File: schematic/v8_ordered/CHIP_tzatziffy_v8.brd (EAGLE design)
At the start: 40.9 x 49.8 mm, 61 parts, among them J1 2X20-CHIP0.8_DRILL_0.15OFFSET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, J2 USB-MICROB", Q2 n.a. / 2N7002ET1G, U1 n.a. / LMR62421, U3 DS2431P, X1 FH12-40S-0.5SH

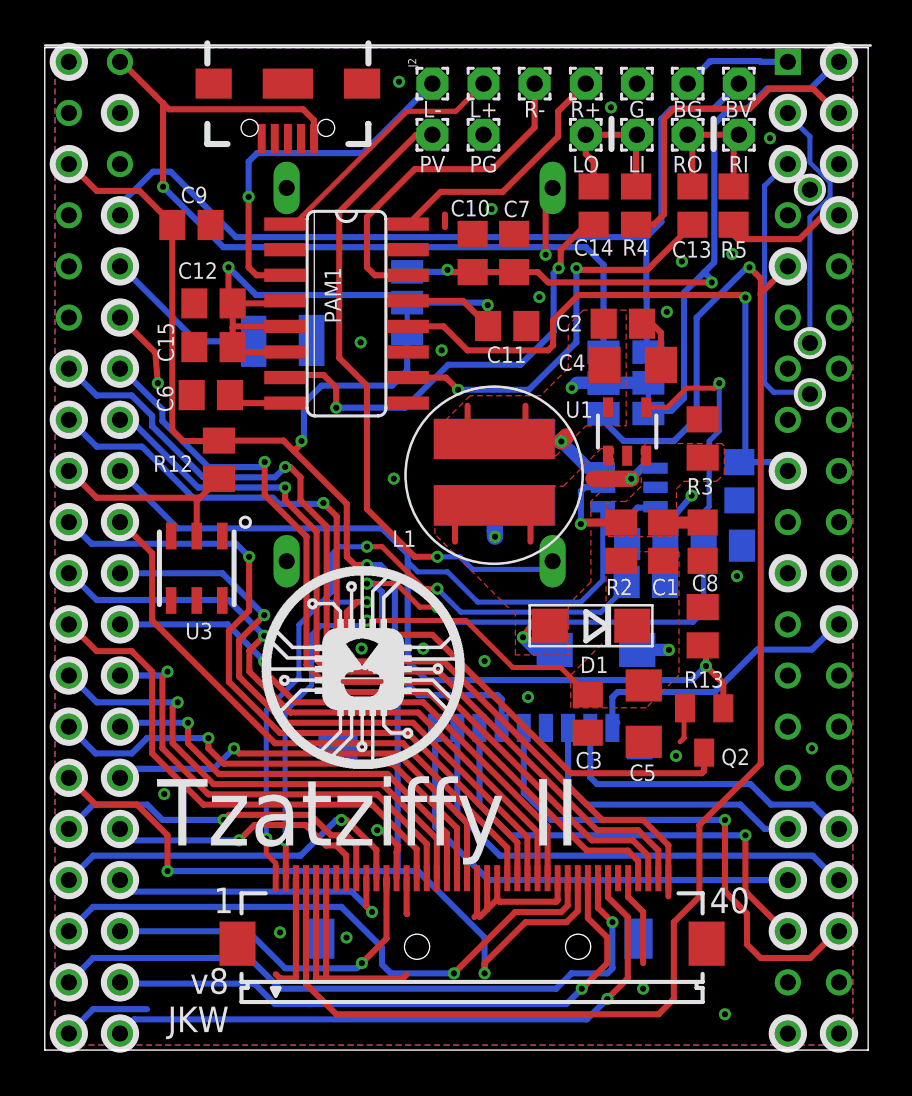
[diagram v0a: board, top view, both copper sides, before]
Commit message: changed chip footprint to clamp via row claming 0.1mm outside and ordered v8
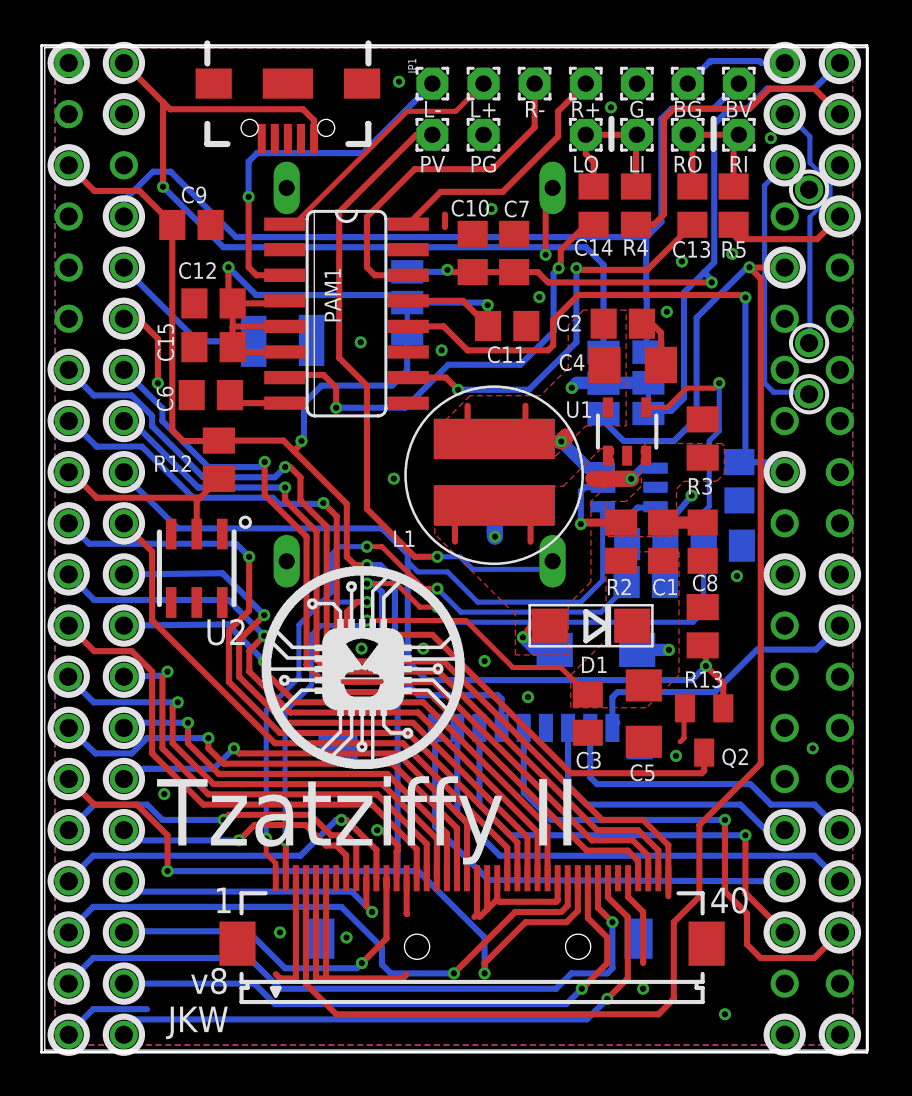
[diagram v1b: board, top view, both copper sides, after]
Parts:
- removed U3: DS2431P, Keyboard v0_5:TSOC6
- added U2: DS2431P, JKW_CHIP:TSOC6
- J1: value 2X20-CHIP0.8_DRILL_0.15OFFSET_LR -> 2X20-CHIP0.9DRILLS_2; device JKW_CHIP:2X20CHIP_0.15MM_OFFSET_TH_08 -> JKW_CHIP:2X20CHIP_BANK_OFFSET_TH_0.9
- JP1: value USB-MICROB" -> USBMICRO_SMD
- renumbered J2 to JP1
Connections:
- net 1WIRE: now also U2.2; no longer U3.2
- net GND: now also U2.1; no longer U3.1
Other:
- board size 40.9 x 49.8 mm -> 41 x 50 mm

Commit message: added and gate
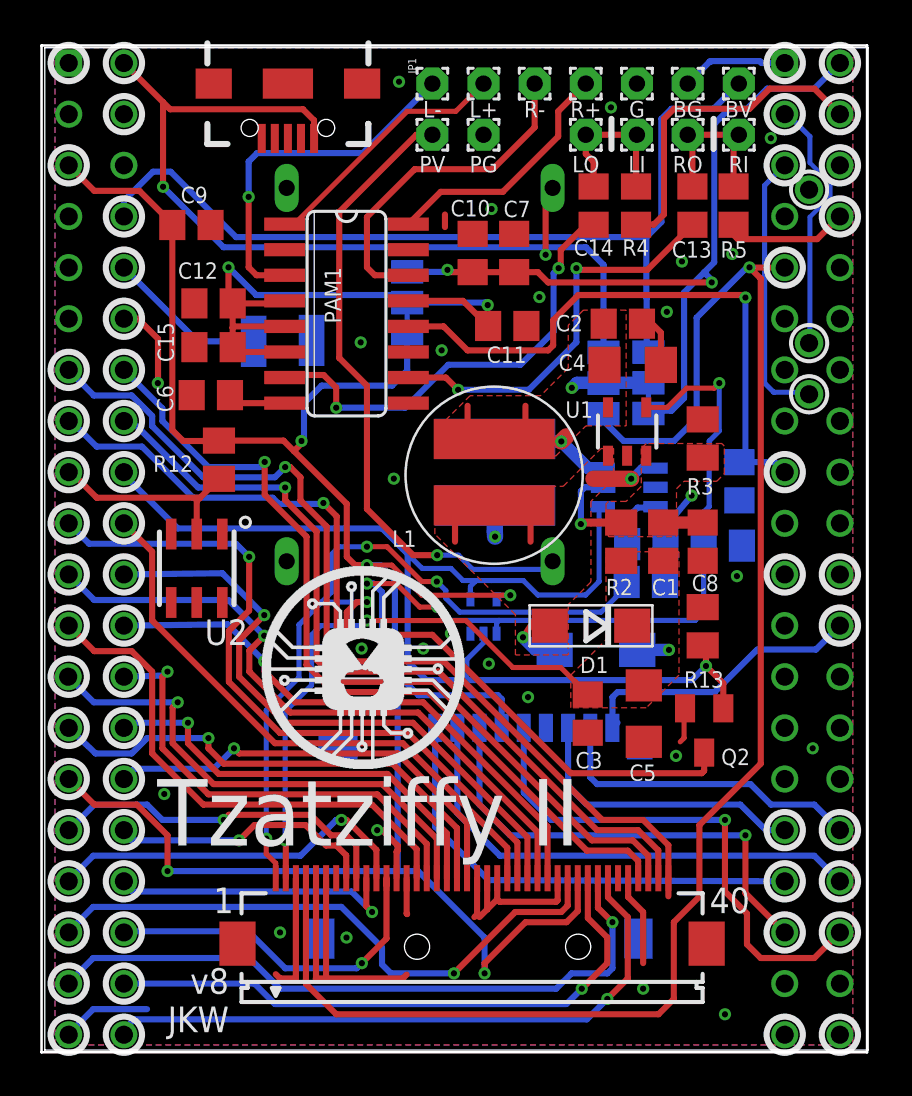
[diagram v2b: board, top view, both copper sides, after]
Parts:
- added IC1: 74AHC1G08DCK, 74xx-little-us:SC70-5
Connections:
- net EN: now also IC1.1
- net GND: now also IC1.3
- net PWM: now also IC1.2, IC1.4
- net VCC3V3: now also IC1.5
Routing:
- net VCC3V3: track 55.4 -> 64.0 mm, vias 2 -> 3
- net PWM: track 55.0 -> 59.5 mm
- net EN: track 83.6 -> 84.2 mm
- net GND: vias 27 -> 28
